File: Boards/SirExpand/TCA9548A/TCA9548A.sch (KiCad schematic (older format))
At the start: 10 parts, among them J1 Conn_01x12, J2 Conn_01x12, U1 TCA9548APWR

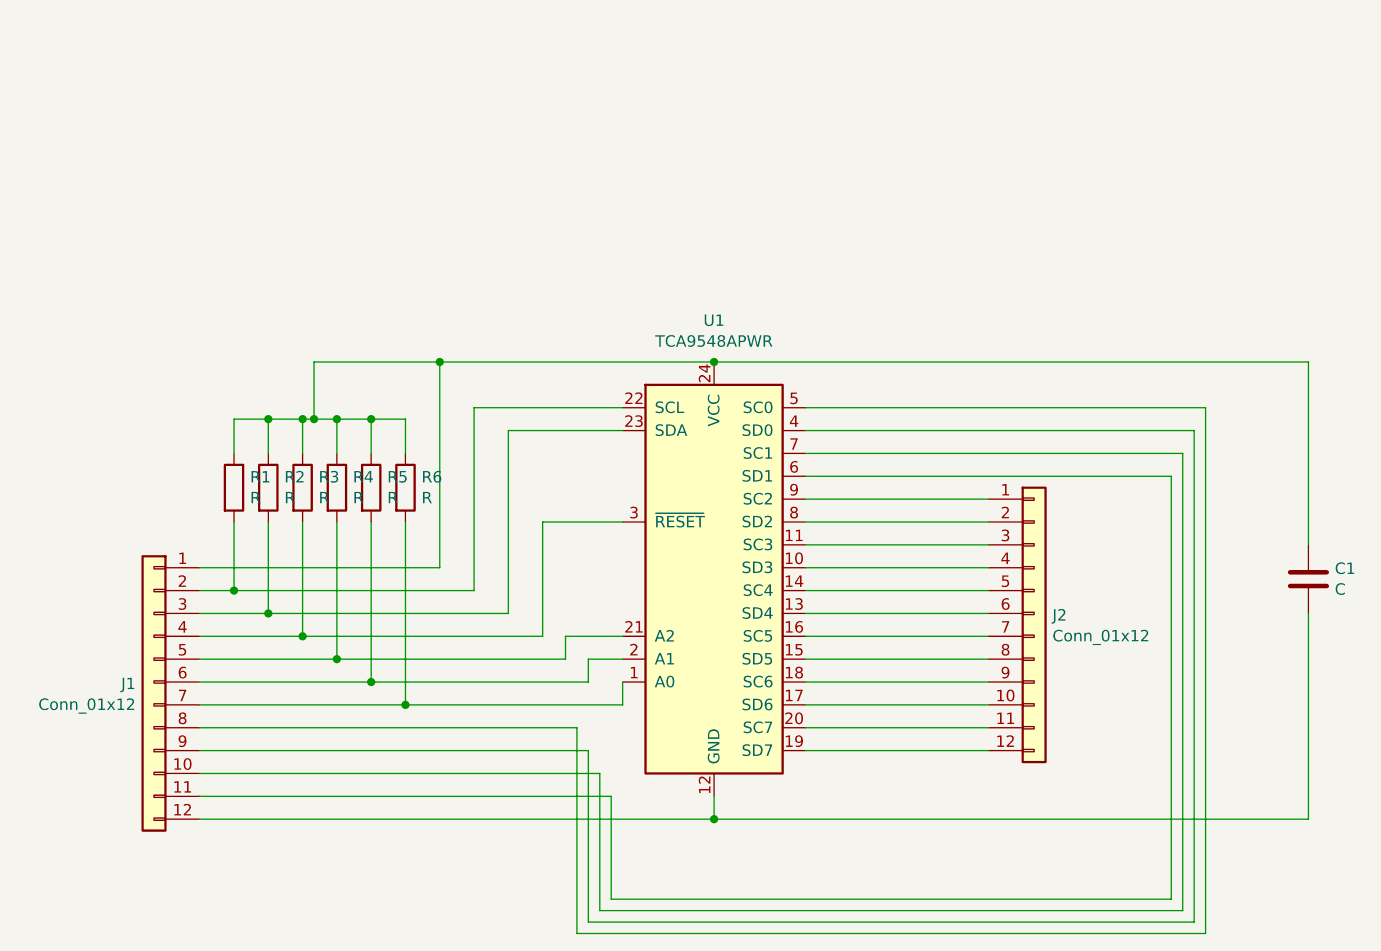
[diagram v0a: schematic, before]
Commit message: TCA9548A Added
Initial Commit
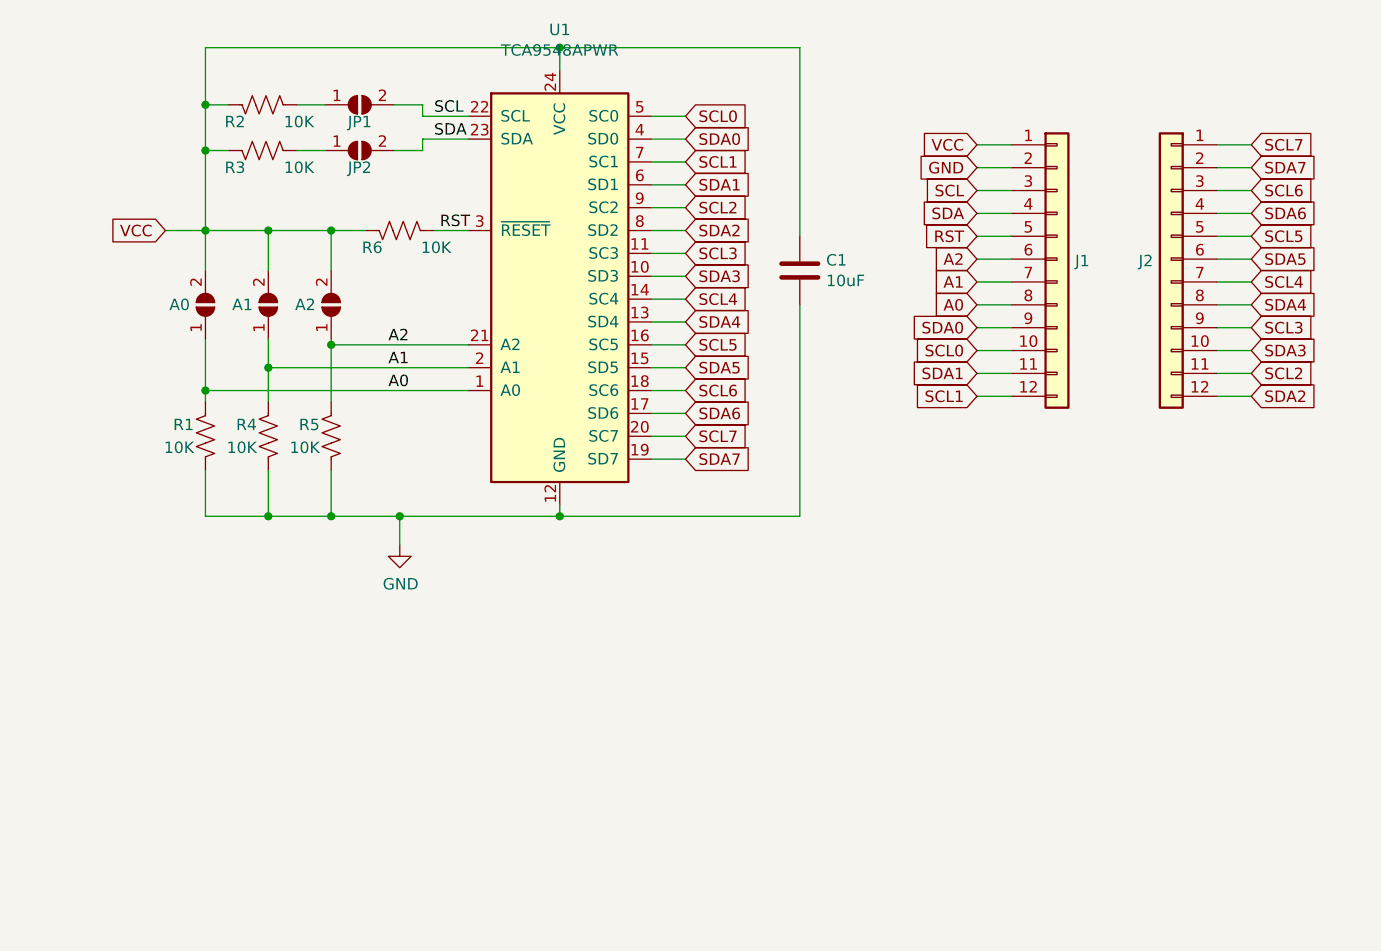
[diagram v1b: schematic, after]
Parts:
- removed R1, R2, R3, R4, R5, R6: R, symbol Device:R
- added A0, A1, A2, JP1, JP2: SolderJumper_2_Open, Jumper:SolderJumper-2_P1.3mm_Open_RoundedPad1.0x1.5mm, symbol Jumper:SolderJumper_2_Open
- added R1, R2, R3, R4, R5, R6: 10K, Resistor_SMD:R_0603_1608Metric, symbol Device:R_US
- C1: value C -> 10uF; footprint (none) -> Capacitor_SMD:C_0805_2012Metric
- J1, J2: footprint (none) -> Connector_PinHeader_2.54mm:PinHeader_1x12_P2.54mm_Vertical
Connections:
- net A0: now reaches U1.1 (A0)
- net A0: now also J1.8 (Pin_8), A0.1 (A), R1.1; no longer J1.7 (Pin_7)
- net SDA3: now reaches U1.10 (SD3)
- net SDA3: now also J2.10 (Pin_10); no longer J2.4 (Pin_4)
- net SCL3: now reaches U1.11 (SC3)
- net SCL3: now also J2.9 (Pin_9); no longer J2.3 (Pin_3)
- net GND: now reaches C1.2, U1.12 (GND)
- net GND: now also J1.2 (Pin_2), R1.2, R4.2, R5.2; no longer J1.12 (Pin_12)
- net SDA4: now reaches U1.13 (SD4)
- net SDA4: now also J2.8 (Pin_8); no longer J2.6 (Pin_6)
- net SCL4: now reaches U1.14 (SC4)
- net SCL4: now also J2.7 (Pin_7); no longer J2.5 (Pin_5)
- net SDA5: now reaches U1.15 (SD5)
- net SDA5: now also J2.6 (Pin_6); no longer J2.8 (Pin_8)
- net SCL5: now reaches U1.16 (SC5)
- net SCL5: now also J2.5 (Pin_5); no longer J2.7 (Pin_7)
- net SDA6: now reaches U1.17 (SD6)
- net SDA6: now also J2.4 (Pin_4); no longer J2.10 (Pin_10)
- net SCL6: now reaches U1.18 (SC6)
- net SCL6: now also J2.3 (Pin_3); no longer J2.9 (Pin_9)
- net SDA2: now reaches J2.12 (Pin_12)
- net SDA2: now also U1.8 (SD2); no longer U1.19 (SD7)
- net A1: now reaches U1.2 (A1)
- net A1: now also J1.7 (Pin_7), A1.1 (A), R4.1; no longer J1.6 (Pin_6)
- net SCL2: now reaches J2.11 (Pin_11)
- net SCL2: now also U1.9 (SC2); no longer U1.20 (SC7)
- net A2: now reaches U1.21 (A2)
- net A2: now also J1.6 (Pin_6), A2.1 (A), R5.1; no longer J1.5 (Pin_5)
- net SCL: now reaches U1.22 (SCL)
- net SCL: now also J1.3 (Pin_3), JP1.2 (B); no longer J1.2 (Pin_2)
- net SDA: now reaches U1.23 (SDA)
- net SDA: now also J1.4 (Pin_4), JP2.2 (B); no longer J1.3 (Pin_3)
- net VCC: now reaches C1.1, J1.1 (Pin_1), U1.24 (VCC)
- net VCC: now also A0.2 (B), A1.2 (B), A2.2 (B), R2.1, R3.1, R6.1
- net RST: now reaches U1.3 (~RESET)
- net RST: now also J1.5 (Pin_5), R6.2; no longer J1.4 (Pin_4)
- net SDA0: now reaches J1.9 (Pin_9), U1.4 (SD0)
- net SCL0: now reaches U1.5 (SC0)
- net SCL0: now also J1.10 (Pin_10); no longer J1.8 (Pin_8)
- net SDA1: now reaches J1.11 (Pin_11), U1.6 (SD1)
- net SCL1: now reaches U1.7 (SC1)
- net SCL1: now also J1.12 (Pin_12); no longer J1.10 (Pin_10)
- net SDA7: now reaches J2.2 (Pin_2)
- net SDA7: now also U1.19 (SD7); no longer U1.8 (SD2)
- net SCL7: now reaches J2.1 (Pin_1)
- net SCL7: now also U1.20 (SC7); no longer U1.9 (SC2)
- new net: JP2.1 (A), R3.2
- new net: JP1.1 (A), R2.2
